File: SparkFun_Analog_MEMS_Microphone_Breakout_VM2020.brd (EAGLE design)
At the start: 14 x 10.2 mm, 25 parts

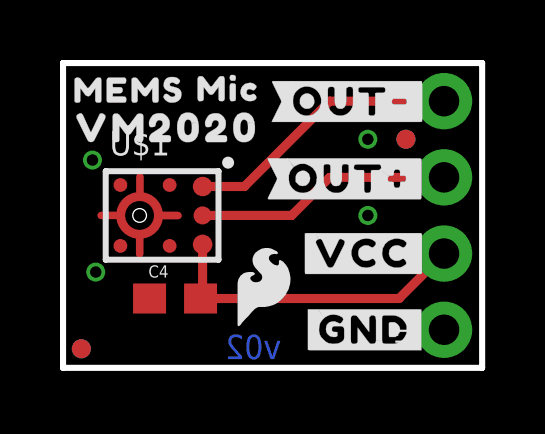
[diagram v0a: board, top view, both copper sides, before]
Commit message: add prod_id to mic
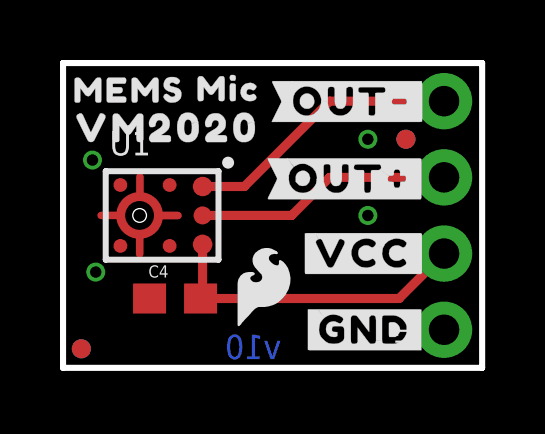
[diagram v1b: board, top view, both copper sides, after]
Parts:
- added LOGO4: SPECIAL_INSTRUCTIONS-ORDERING, SparkFun-Aesthetics:ORDERING_INSTRUCTIONS
- renumbered U$1 to U1
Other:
- board text added: "Board Thickness is 1.6mm"
- board text added: "v10"
- board text removed: "v02"
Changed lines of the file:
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@@
 <drawing>
 <settings>
-<setting alwaysvectorfont="yes"/>
+<setting alwaysvectorfont="no"/>
 <setting keepoldvectorfont="yes"/>
 <setting verticaltext="up"/>
 </settings>
-<grid distance="0.05" unitdist="inch" unit="inch" style="lines" multiple="1" display="yes" altdistance="0.0001" altunitdist="inch" altunit="inch"/>
+<grid distance="0.05" unitdist="inch" unit="inch" style="lines" multiple="1" display="yes" altdistance="0.005" altunitdist="inch" altunit="inch"/>
 <layers>
 <layer number="1" name="Top" color="4" fill="1" visible="yes" active="yes"/>
@@
 <layer number="45" name="Holes" color="7" fill="1" visible="yes" active="yes"/>
 <layer number="46" name="Milling" color="3" fill="1" visible="no" active="yes"/>
-<layer number="47" name="Measures" color="7" fill="1" visible="no" active="yes"/>
+<layer number="47" name="Measures" color="7" fill="1" visible="yes" active="yes"/>
 <layer number="48" name="Document" color="7" fill="1" visible="no" active="yes"/>
 <layer number="49" name="Reference" color="7" fill="1" visible="yes" active="yes"/>
@@
 <layer number="98" name="Guide" color="6" fill="1" visible="no" active="no"/>
 <layer number="99" name="SpiceOrder" color="7" fill="1" visible="no" active="no"/>
-<layer number="100" name="Muster" color="7" fill="1" visible="no" active="yes"/>
+<layer number="100" name="Muster" color="7" fill="1" visible="yes" active="yes"/>
 <layer number="101" name="Patch_Top" color="12" fill="4" visible="no" active="yes"/>
 <layer number="102" name="Vscore" color="7" fill="1" visible="no" active="yes"/>
@@
 <text x="1.27" y="-1.778" size="1.016" layer="27" font="vector">Mic Breakout</text>
 <text x="11.43" y="-11.43" size="1.778" layer="51" font="vector" ratio="9">Pete Lewis</text>
-<text x="6.3373" y="0.2921" size="0.8128" layer="16" font="vector" ratio="20" rot="SMR0" align="bottom-center">v02</text>
+<text x="6.3373" y="0.2921" size="0.8128" layer="16" font="vector" ratio="20" rot="SMR0" align="bottom-center">v10</text>
 <dimension x1="0" y1="10.16" x2="0" y2="0" x3="-7.62" y3="5.08" textsize="1.27" textratio="15" layer="47" width="0.0762" unit="inch" precision="3"/>
 <dimension x1="13.97" y1="10.16" x2="0" y2="10.16" x3="6.985" y3="17.78" textsize="1.27" textratio="15" layer="47" width="0.0762" unit="inch" precision="3"/>
-<dimension x1="13.97" y1="0" x2="12.7" y2="2.54" x3="21.59" y3="1.27" textsize="1.27" textratio="15" layer="47" dtype="vertical" width="0.0762" unit="inch" precision="3"/>
-<dimension x1="13.97" y1="0" x2="12.7" y2="5.08" x3="17.78" y3="2.54" textsize="1.27" textratio="15" layer="47" dtype="vertical" width="0.0762" unit="inch" precision="3"/>
-<dimension x1="0" y1="0" x2="2.54" y2="3.81" x3="1.27" y3="13.97" textsize="1.27" textratio="15" layer="47" dtype="horizontal" width="0.0762" unit="inch" precision="3"/>
-<dimension x1="0" y1="0" x2="2.54" y2="3.81" x3="-3.81" y3="1.905" textsize="1.27" textratio="15" layer="47" dtype="vertical" width="0.0762" unit="inch"/>
-<text x="-2.54" y="22.86" size="1.27" layer="47" font="vector">Units: INCHES</text>
+<dimension x1="11.43" y1="8.89" x2="12.7" y2="6.35" x3="16.51" y3="7.62" textsize="1.27" textratio="15" layer="47" dtype="vertical" width="0.0762" unit="inch" precision="3"/>
+<dimension x1="13.97" y1="0" x2="12.7" y2="1.27" x3="20.32" y3="0.635" textsize="1.27" textratio="15" layer="47" dtype="vertical" width="0.0762" unit="inch" precision="3"/>
+<dimension x1="0" y1="0" x2="2.54" y2="5.08" x3="1.27" y3="13.97" textsize="1.27" textratio="15" layer="47" dtype="horizontal" width="0.0762" unit="inch" precision="3"/>
+<dimension x1="0" y1="0" x2="2.54" y2="5.08" x3="-3.81" y3="2.54" textsize="1.27" textratio="15" layer="47" dtype="vertical" width="0.0762" unit="inch"/>
+<text x="0" y="22.86" size="1.27" layer="47" font="vector">Units: INCHES</text>
 <text x="-7.62" y="-13.97" size="1.778" layer="51" font="vector" ratio="9">Based on a MEMs mic design by Pete Dokter</text>
+<text x="24.13" y="38.1" size="1.778" layer="51" font="vector" ratio="15">Board Thickness is 1.6mm</text>
 </plain>
 <attributes>
@@
 <element name="FD4" library="SparkFun-Aesthetics" package="FIDUCIAL-MICRO" value="FIDUCIALUFIDUCIAL" x="0.6096" y="0.635" smashed="yes" rot="MR0"/>
 <element name="LOGO3" library="SparkFun-Aesthetics" package="SFE_LOGO_FLAME_.1" value="SFE_LOGO_FLAME.1_INCH" x="6.677659375" y="2.7178" smashed="yes"/>
-<element name="U$1" library="vm2020" package="VM2020" value="VM2020" x="3.302" y="5.08" smashed="yes">
+<element name="U1" library="vm2020" package="VM2020" value="VM2020" x="3.302" y="5.08" smashed="yes">
 <attribute name="DIGIKEY_PART" value="" x="3.302" y="5.08" size="1.778" layer="27" font="vector" ratio="15" display="off"/>
 <attribute name="MANU_PART" value="VM2020" x="3.302" y="5.08" size="1.778" layer="27" font="vector" ratio="15" display="off"/>
 <attribute name="NAME" x="1.552" y="7.08" size="0.8128" layer="25"/>
-<attribute name="PROD_ID" value="" x="3.302" y="5.08" size="1.778" layer="27" font="vector" ratio="15" display="off"/>
+<attribute name="PROD_ID" value="IC-17514" x="3.302" y="5.08" size="1.778" layer="27" font="vector" ratio="15" display="off"/>
 <attribute name="VALUE" x="1.552" y="2.58" size="0.8128" layer="27"/>
 </element>
@@
 <element name="U$7" library="output" package="MEMS23" value="" x="3.3909" y="8.89" smashed="yes" rot="MR0"/>
 <element name="U$16" library="output" package="MIC24" value="" x="3.48741875" y="7.693659375" smashed="yes" rot="MR0"/>
+<element name="LOGO4" library="SparkFun-Aesthetics" package="ORDERING_INSTRUCTIONS" value="SPECIAL_INSTRUCTIONS-ORDERING" x="22.86" y="50.8" smashed="yes"/>
 </elements>
 <signals>
@@
 <via x="10.16" y="7.62" extent="1-16" drill="0.381"/>
 <via x="10.16" y="5.08" extent="1-16" drill="0.381"/>
-<contactref element="U$1" pad="3"/>
-<contactref element="U$1" pad="4"/>
-<contactref element="U$1" pad="8"/>
-<contactref element="U$1" pad="2"/>
-<contactref element="U$1" pad="5"/>
+<contactref element="U1" pad="3"/>
+<contactref element="U1" pad="4"/>
+<contactref element="U1" pad="8"/>
+<contactref element="U1" pad="2"/>
+<contactref element="U1" pad="5"/>
 <wire x1="1.922" y1="5.08" x2="1.27" y2="5.08" width="0.254" layer="1"/>
 <wire x1="2.555240625" y1="4.4518375" x2="2.555240625" y2="3.7998375" width="0.254" layer="1"/>
@@
 <signal name="VCC">
 <contactref element="C4" pad="2"/>
-<contactref element="U$1" pad="6"/>
+<contactref element="U1" pad="6"/>
 <contactref element="J1" pad="2"/>
 <wire x1="12.7" y1="3.81" x2="11.2014" y2="2.3114" width="0.3048" layer="1"/>
@@
 </signal>
 <signal name="OUT-">
-<contactref element="U$1" pad="1"/>
+<contactref element="U1" pad="1"/>
 <contactref element="J1" pad="4"/>
 <wire x1="4.652" y1="6.045" x2="6.045" y2="6.045" width="0.3048" layer="1"/>
@@
 </signal>
 <signal name="OUT+">
-<contactref element="U$1" pad="7"/>
+<contactref element="U1" pad="7"/>
 <contactref element="J1" pad="3"/>
 <wire x1="4.652" y1="5.08" x2="7.62" y2="5.08" width="0.3048" layer="1"/>
